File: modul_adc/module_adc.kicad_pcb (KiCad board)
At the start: 2 copper layers, 61 x 55.9 mm, 28 parts

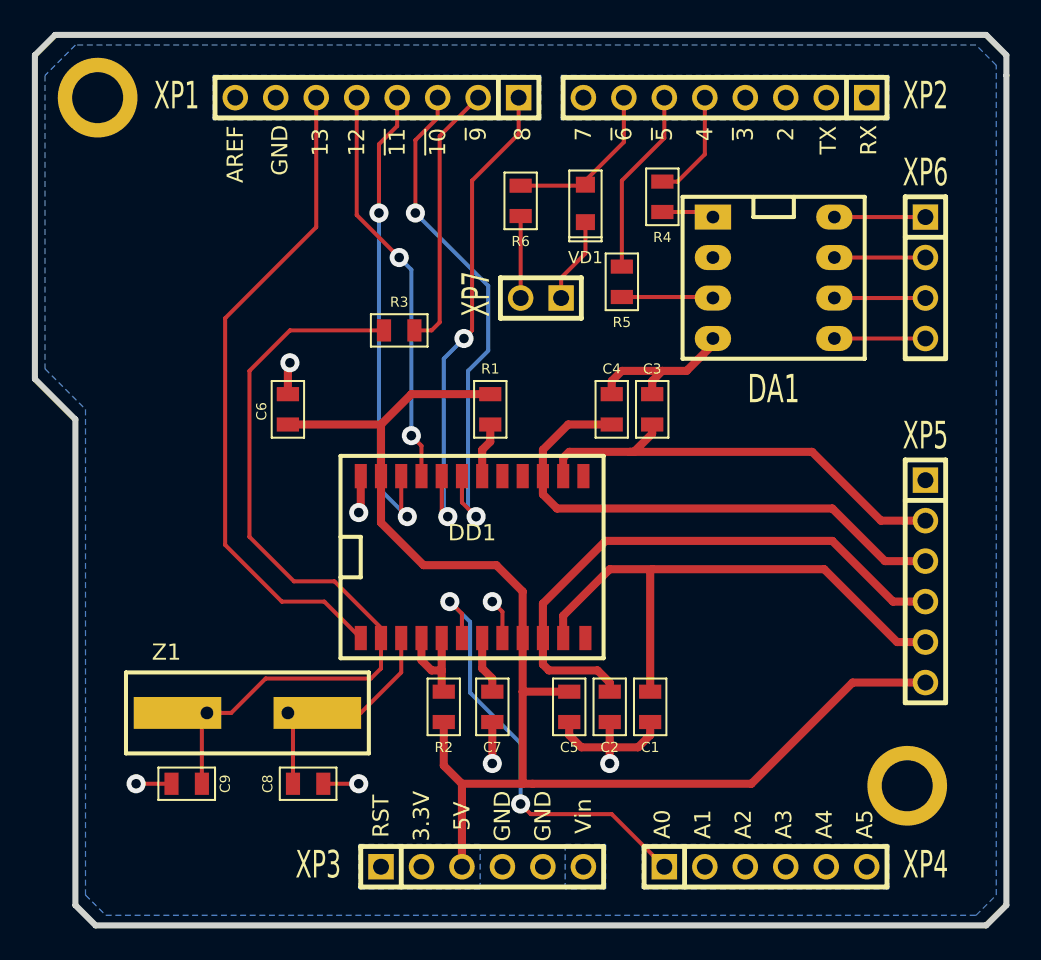
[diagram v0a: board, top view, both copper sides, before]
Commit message: Поправил шелкографию и добавил номиналы у элементов для adc_module.
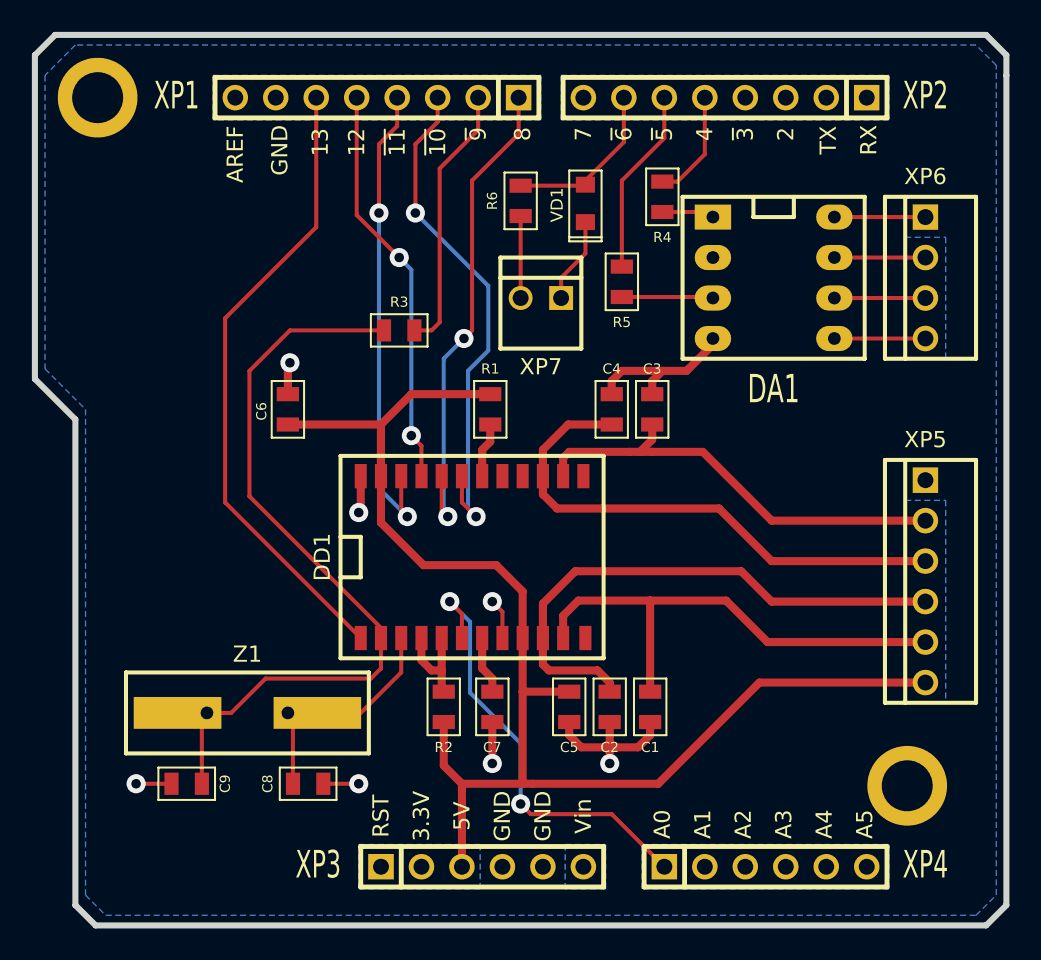
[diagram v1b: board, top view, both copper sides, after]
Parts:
- C1, C2, C3, C4, C5, C6, C7: value 0.1_мк -> 0.1 мк
- C8, C9: value ~ -> 12 п
- R1, R2: value 1_k -> 1 к
- R6: value 1_к -> 1 к
- XP5: footprint SIL-6 -> WF-6
- XP6: footprint SIL-4 -> WF-4
- XP7: footprint SIL-2 -> WF-2
- Z1: value ~ -> 2.4576 МГц
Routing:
- net /AIN1-: track 35.0 -> 31.3 mm
- net /AIN1+: track 36.3 -> 34.7 mm
- net /PB5: track 41.4 -> 39.8 mm
- net N-0000046: track 50.0 -> 48.5 mm

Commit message: Восстановил проект для работы в kicad 7.0.
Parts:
- C1, C2, C3, C4, C5, C6, C7, C8, C9, R1, R2, R3, R4, R5, R6: footprint SMD0805 -> IWsmd_case:SMD0805
- DA1: footprint DIP_8 -> IWcomponents:DIP_8
- DD1: footprint SOIC_24 -> IWsmd_case:SOIC_24
- VD1: footprint SOD110 -> IWcomponents:SOD110
- XP1, XP2: footprint SIL-8 -> IWconnectors:PIN_ARRAY_8x1
- XP3, XP4: footprint SIL-6 -> IWconnectors:PIN_ARRAY_6x1
- XP5: footprint WF-6 -> IWconnectors:WF-6
- XP6: footprint WF-4 -> IWconnectors:WF-4
- XP7: footprint WF-2 -> IWconnectors:WF-2
- Z1: footprint Q_49U3HMS& -> IWcomponents:Q_49U3HMS&
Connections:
- DD1 pad 12: (no net) -> unconnected-(DD1-AIN2(+)/D1-Pad12)
- DD1 pad 13: (no net) -> unconnected-(DD1-AIN2(-)/D0-Pad13)
- DD1 pad 16: (no net) -> unconnected-(DD1-ACX-Pad16)
- DD1 pad 17: (no net) -> unconnected-(DD1-~{ACX}-Pad17)
- XP1 pad 3: /PB2 -> /SS
- XP1 pad 4: /PB3 -> /MOSI
- XP1 pad 5: /PB4 -> /MISO
- XP1 pad 6: /PB5 -> /SCK
- XP1 pad 7: (no net) -> /GND
- XP1 pad 8: (no net) -> /AREF
- XP2 pad 1: (no net) -> /RXD
- XP2 pad 2: (no net) -> /TXD
- XP2 pad 3: (no net) -> /PD2
- XP2 pad 4: (no net) -> /PD3
- XP2 pad 8: (no net) -> /PD7
- XP3 pad 1: (no net) -> unconnected-(XP3-Pad1)
- XP3 pad 2: (no net) -> unconnected-(XP3-Pad2)
- XP3 pad 6: (no net) -> unconnected-(XP3-Pad6)
- XP4 pad 2: (no net) -> /A1
- XP4 pad 3: (no net) -> /A2
- XP4 pad 4: (no net) -> /A3
- XP4 pad 5: (no net) -> /A4
- XP4 pad 6: (no net) -> /A5
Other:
- net class Default removed
- board text added: "~{10}"
- board text added: "~{11}"
- board text added: "~{3}"
- board text added: "~{5}"
- board text added: "~{6}"
- board text added: "~{9}"
- board text removed: "~10"
- board text removed: "~11"
- board text removed: "~3"
- board text removed: "~5"
- board text removed: "~6"
- board text removed: "~9"

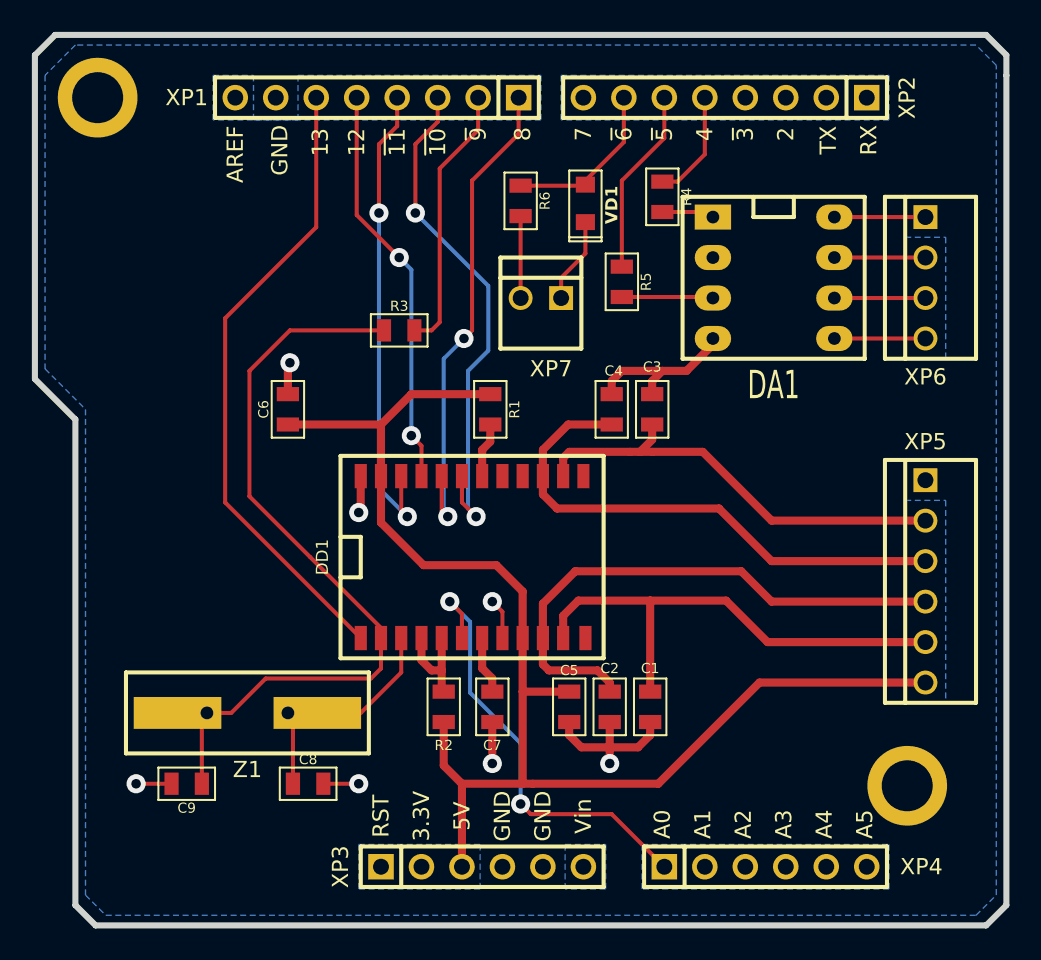
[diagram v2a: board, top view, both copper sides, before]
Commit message: Дополнил схему ацп для тензодатчика и приступил к трассировке печатной платы.
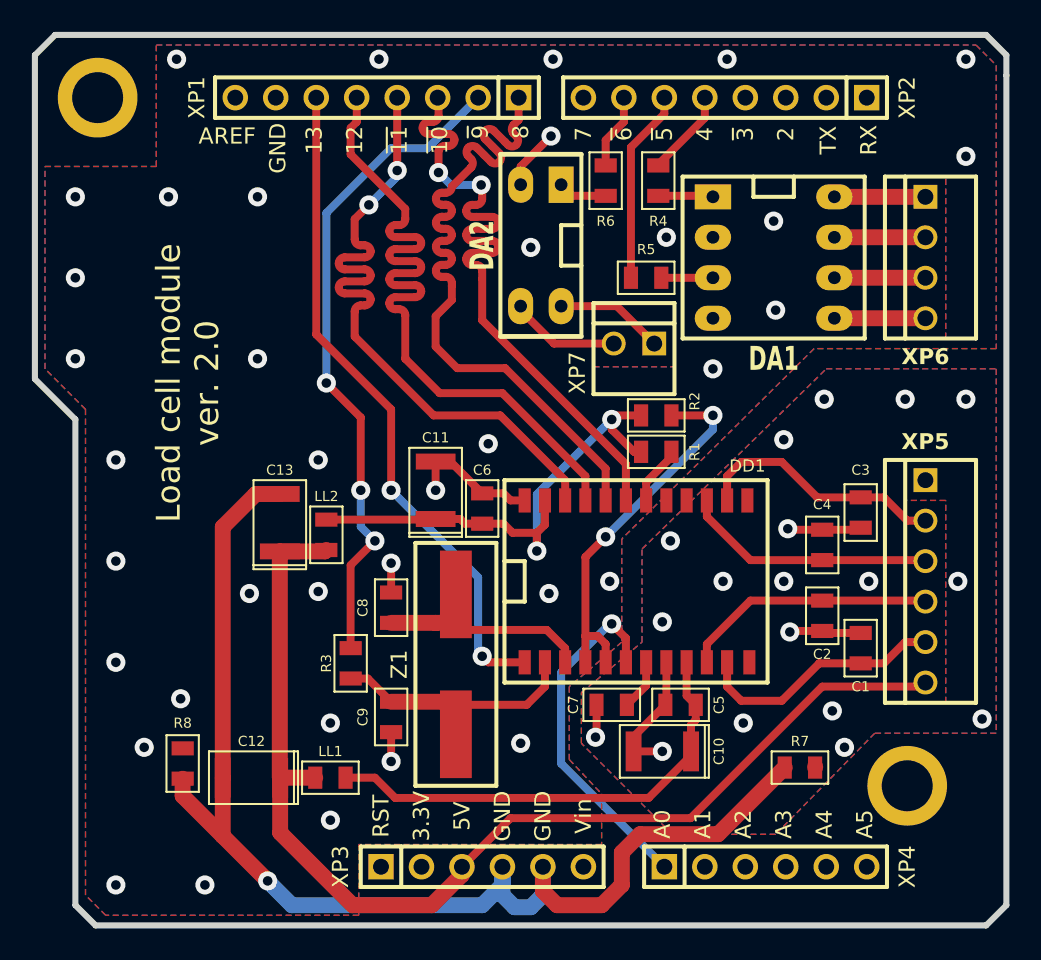
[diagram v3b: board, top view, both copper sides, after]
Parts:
- removed VD1: BAS216, IWcomponents:SOD110
- added C10: 10 мк 10В, IWsmd_case:CASE_B, F.Cu at (104.1, 137.7)
- added C11: 10 мк 10В, IWsmd_case:CASE_B, F.Cu at (89.9, 121.3)
- added C12: 10 мк 10В, IWsmd_case:CASE_B, F.Cu at (78.4, 139.3)
- added C13: 10 мк 10В, IWsmd_case:CASE_B, F.Cu at (80.1, 123.3)
- added DA2: TLP521-1, IWcomponents:DIP_4, F.Cu at (96.5, 105.9)
- added LL1: 47 мк, IWsmd_case:SMD0805, F.Cu at (83.3, 139.3)
- added LL2: 47 мк, IWsmd_case:SMD0805, F.Cu at (83.1, 124.1)
- added R7: 0, IWsmd_case:SMD0805, F.Cu at (112.8, 138.7)
- added R8: 0, IWsmd_case:SMD0805, F.Cu at (74.0, 138.4)
- DD1: value AD7730 -> AD7730BR
- R6: value 1 к -> 470
- Z1: value 2.4576 МГц -> 4.9152 МГц; footprint IWcomponents:Q_49U3HMS& -> IWcomponents:HC-49SM
- moved R2 22.6 mm to (103.8, 116.6), turned to 0 degrees
- moved R3 21.1 mm to (84.6, 132.1), turned to 90 degrees
- moved C4 15.7 mm to (114.2, 124.7)
- moved C3 14.6 mm to (116.6, 122.7), turned to -90 degrees
- moved C2 14.5 mm to (114.2, 129.2)
- moved C1 13.7 mm to (116.6, 131.2), turned to -90 degrees
- moved C6 13.7 mm to (92.8, 122.4)
- moved C9 13.5 mm to (87.1, 135.5), turned to -90 degrees
- moved Z1 13.4 mm to (91.2, 132.2), turned to -90 degrees
- moved C8 12.2 mm to (87.1, 128.7), turned to 90 degrees
- moved R1 10.8 mm to (103.8, 118.9), turned to 0 degrees
- moved DD1 10.4 mm to (102.5, 127.0)
- moved C7 7.49 mm to (101.0, 134.7), turned to 0 degrees
- moved C5 6.99 mm to (105.3, 134.7), turned to 180 degrees
- moved XP7 6.50 mm to (102.4, 112.1)
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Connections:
- C1 pad 1: /GND -> /AGND
- C2 pad 1: /GND -> /AGND
- C3 pad 2: /GND -> /AGND
- C4 pad 2: /GND -> /AGND
- C5 pad 1: /+5V -> Net-(DD1-AVdd)
- C5 pad 2: /GND -> /AGND
- C6 pad 1: /+5V -> Net-(DD1-DVdd)
- C6 pad 2: /GND -> /DGND
- C7 pad 1: /GND -> /AGND
- C8 pad 2: /GND -> /DGND
- C9 pad 2: /GND -> /DGND
- DA1 pad 2: /GND -> /DGND
- DA1 pad 4: /GND -> /DGND
- DD1 pad 23: /+5V -> Net-(DD1-DVdd)
- DD1 pad 24: /GND -> /DGND
- DD1 pad 8: /GND -> /AGND
- DD1 pad 9: /+5V -> Net-(DD1-AVdd)
- R1 pad 1: /+5V -> Net-(DD1-DVdd)
- R2 pad 1: /+5V -> Net-(DD1-DVdd)
- R6 pad 2: /GND -> Net-(DA2-Pad1)
- XP1 pad 3: /SS -> /PB2
- XP1 pad 4: /MOSI -> /PB3
- XP1 pad 5: /MISO -> /PB4
- XP1 pad 6: /SCK -> /PB5
- XP1 pad 7: /GND -> unconnected-(XP1-Pad7)
- XP5 pad 1: /GND -> /AGND
- XP7 pad 2: /GND -> Net-(DA2-Pad3)
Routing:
- net /GND: track 39.3 -> 78.0 mm, vias 7 -> 1
- net Net-(DD1-MCLK_IN): track 48.5 -> 14.9 mm
- net Net-(DD1-DVdd): track 0.00 -> 32.2 mm, vias 0 -> 2
- net Net-(DD1-AVdd): track 0.00 -> 29.5 mm
- net /PB1: track 16.9 -> 41.7 mm, vias 0 -> 3
- net /PB4: track 25.4 -> 45.0 mm, vias 2 -> 0
- net /AGND: track 0.00 -> 19.5 mm, vias 0 -> 18
- net /AIN1+: track 34.7 -> 16.0 mm
- net Net-(DD1-POL): track 6.35 -> 24.0 mm, vias 0 -> 2
- net /REF_IN-: track 33.5 -> 15.9 mm
- net /DGND: track 0.00 -> 15.9 mm, vias 0 -> 37
- net /AIN1-: track 31.3 -> 15.9 mm
- net /+5V: track 86.6 -> 71.3 mm
- net /PB0: track 31.0 -> 45.0 mm, vias 2 -> 0
- net /REF_IN+: track 27.9 -> 15.9 mm
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- added copper zone on B.Cu, net /AGND
- added copper zone on F.Cu, net /AGND
- added copper zone on B.Cu, net /DGND
- added copper zone on F.Cu, net /DGND
- removed copper zone on B.Cu, net /GND
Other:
- rule pad_to_mask_clearance: 0.254 -> 0.25
- board text added: "Load cell module ver. 2.0"

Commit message: Подготовил печатные платы тензодатчика и 16-ти сегментного индикатора к отправке в производство.
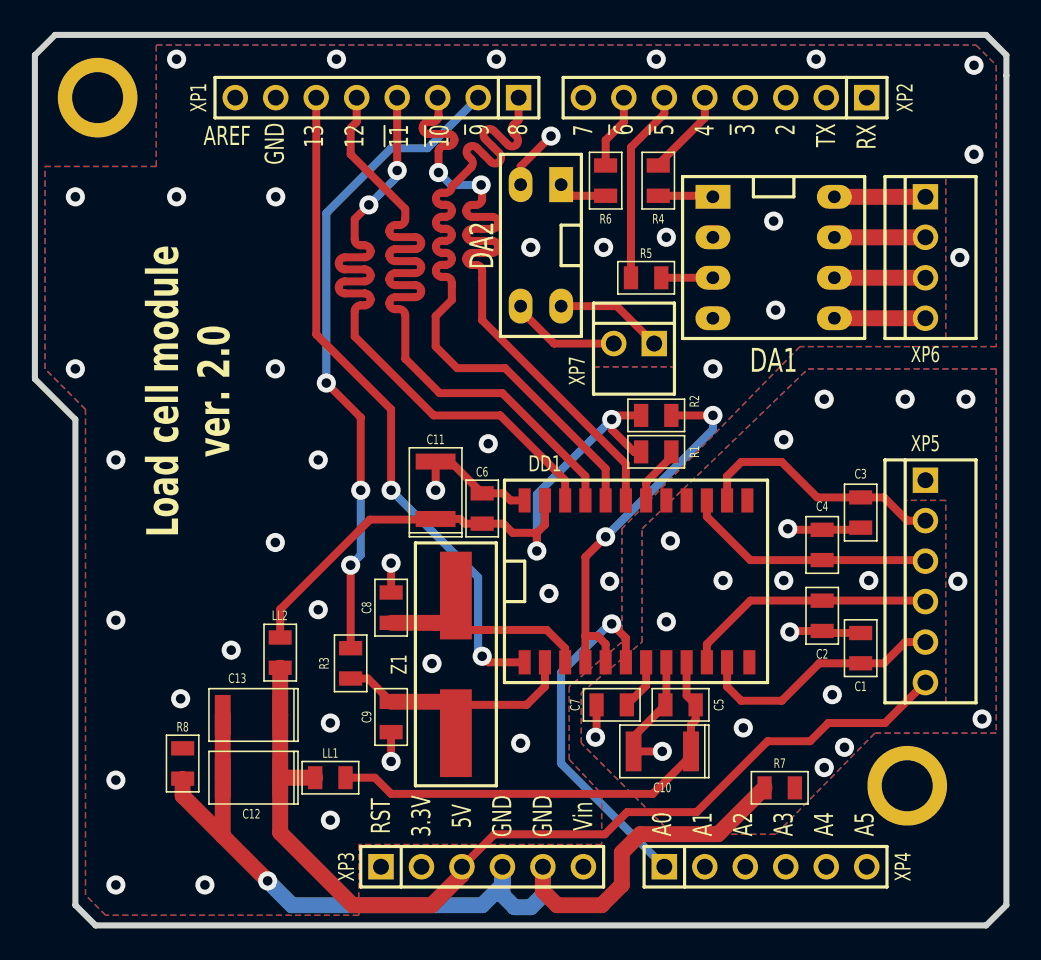
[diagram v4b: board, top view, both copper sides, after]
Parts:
- removed arduino (x2): P***, 1_pin
- added 1_PIN_3_2mm_1: P***, IWconnectors:1_pin_3_2mm, F.Cu at (68.7, 96.6)
- added 1_PIN_3_2mm_2: P***, IWconnectors:1_pin_3_2mm, F.Cu at (119.5, 139.8)
- moved C13 12.2 mm to (78.4, 135.4), turned to 180 degrees
- moved LL2 7.94 mm to (80.2, 131.5)
- moved R7 1.80 mm to (111.5, 140.0)
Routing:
- net /GND: track 78.0 -> 60.0 mm
- net /+5V: track 71.3 -> 61.0 mm
- net Net-(DD1-DVdd): track 32.2 -> 39.2 mm
- net /PB1: track 41.7 -> 41.0 mm
- net /AGND: vias 18 -> 19
- net /DGND: vias 37 -> 40
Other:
- rule pad_to_mask_clearance: 0.25 -> 0.2

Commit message: Добавил обозначение разъёмов на схеме, поправил посадочное место кварца и отправил плату в производство.
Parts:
- Z1: footprint IWcomponents:HC-49SM -> IWcrystal_oscil:HC-49U
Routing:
- net /PB4: track 45.0 -> 46.1 mm
- net /PB5: track 42.2 -> 43.3 mm
- net /PB0: track 45.0 -> 46.0 mm
- net /PB3: track 42.2 -> 43.1 mm
- net /PB2: track 42.1 -> 43.0 mm
- net /PB1: track 41.0 -> 41.8 mm
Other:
- board text added: "9"
- board text removed: "~{9}"
